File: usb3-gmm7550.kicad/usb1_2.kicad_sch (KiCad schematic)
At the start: 0 parts

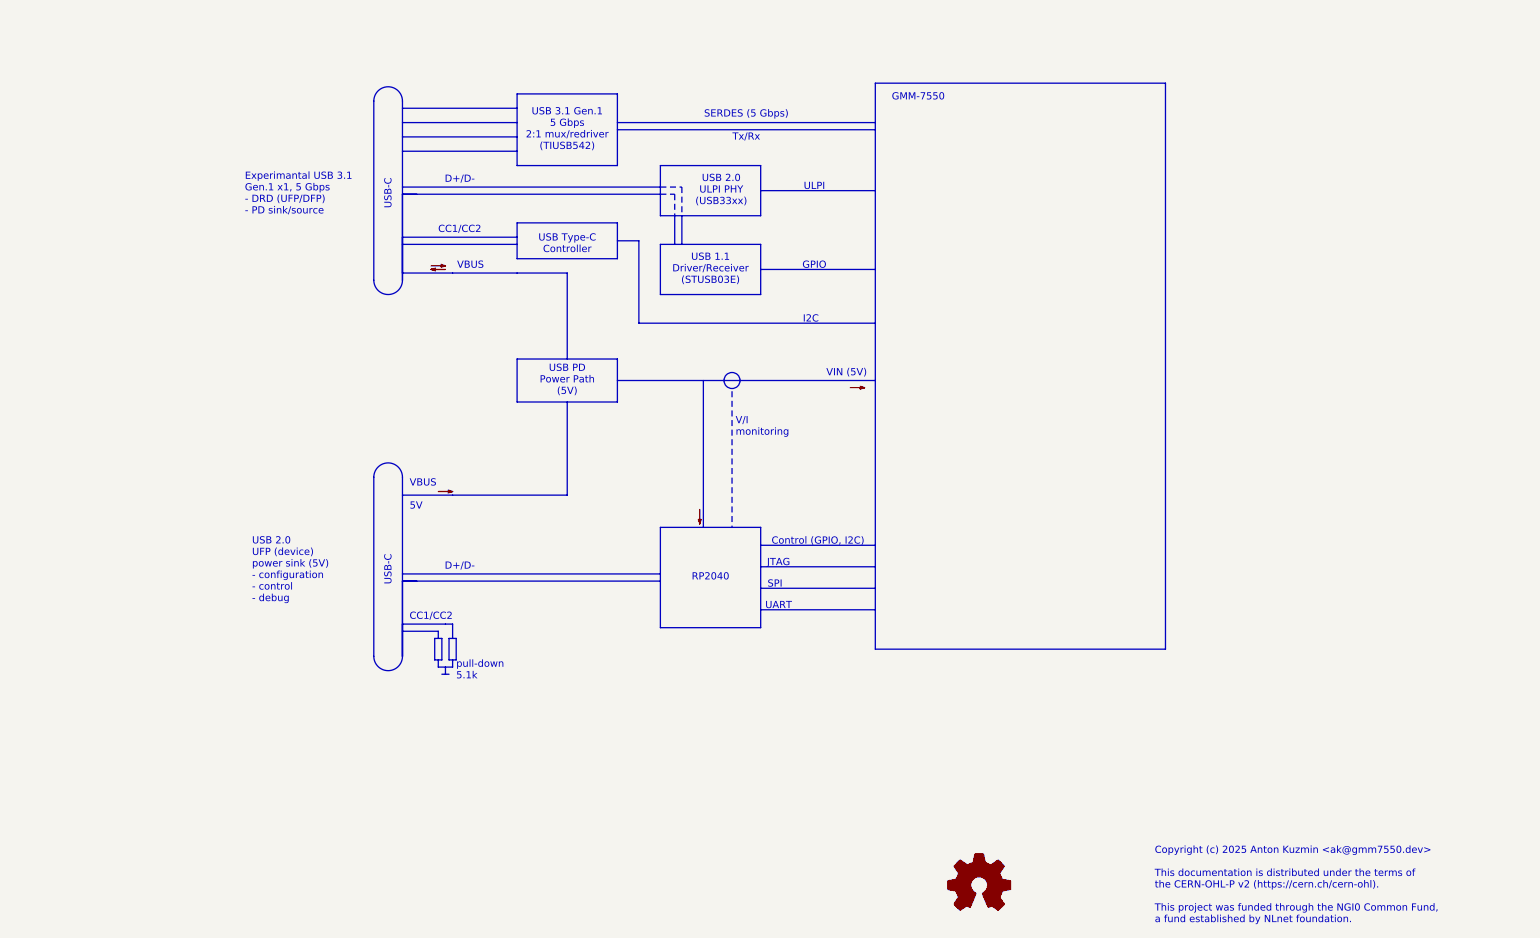
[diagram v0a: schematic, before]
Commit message: Add pages to the USB 3 Adapter schematic and new project symbols
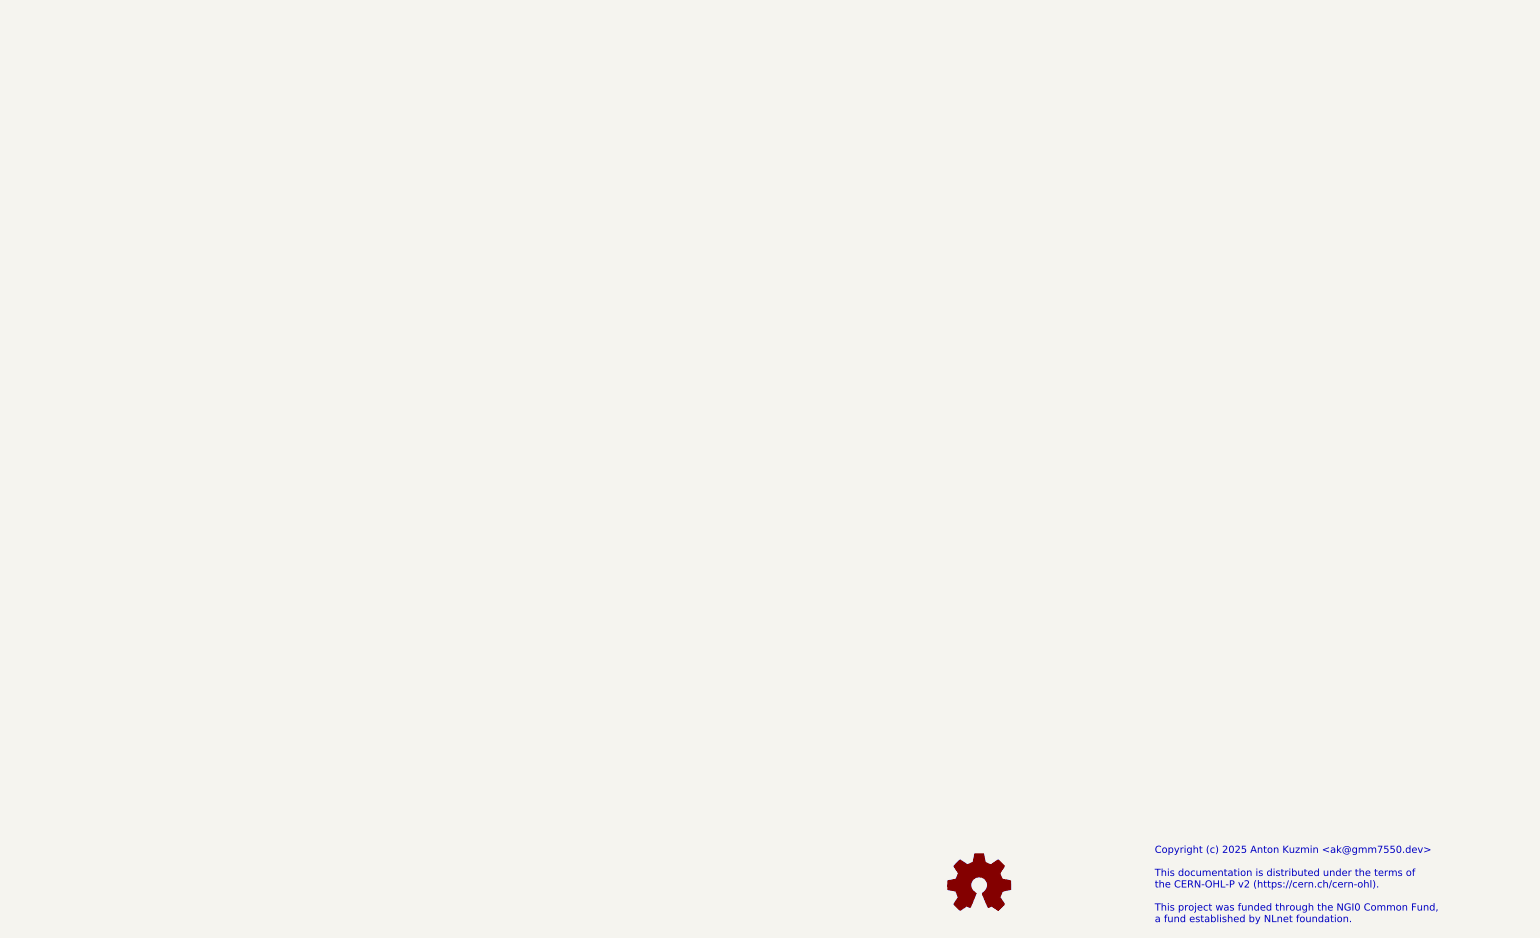
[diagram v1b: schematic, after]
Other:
- note removed: "CC1/CC2"
- note removed: "Control (GPIO, I2C)"
- note removed: "D+/D-"
- note removed: "Experimantal USB 3.1 Gen.1 x1, 5 Gbps - DRD (UFP/DFP) - PD sink/source"
- note removed: "GMM-7550"
- note removed: "GPIO"
- note removed: "I2C"
- note removed: "JTAG"
- note removed: "RP2040"
- note removed: "SERDES (5 Gbps) Tx/Rx"
- note removed: "SPI"
- note removed: "UART"
- note removed: "ULPI"
- note removed: "USB 1.1 Driver/Receiver (STUSB03E)"
- note removed: "USB 2.0 UFP (device) power sink (5V) - configuration - control - debug"
- note removed: "USB 2.0 ULPI PHY (USB33xx)"
- note removed: "USB 3.1 Gen.1 5 Gbps 2:1 mux/redriver (TIUSB542)"
- note removed: "USB PD Power Path (5V)"
- note removed: "USB Type-C Controller"
- note removed: "USB-C"
- note removed: "V/I monitoring"
- note removed: "VBUS"
- note removed: "VBUS 5V"
- note removed: "VIN (5V)"
- note removed: "pull-down 5.1k"

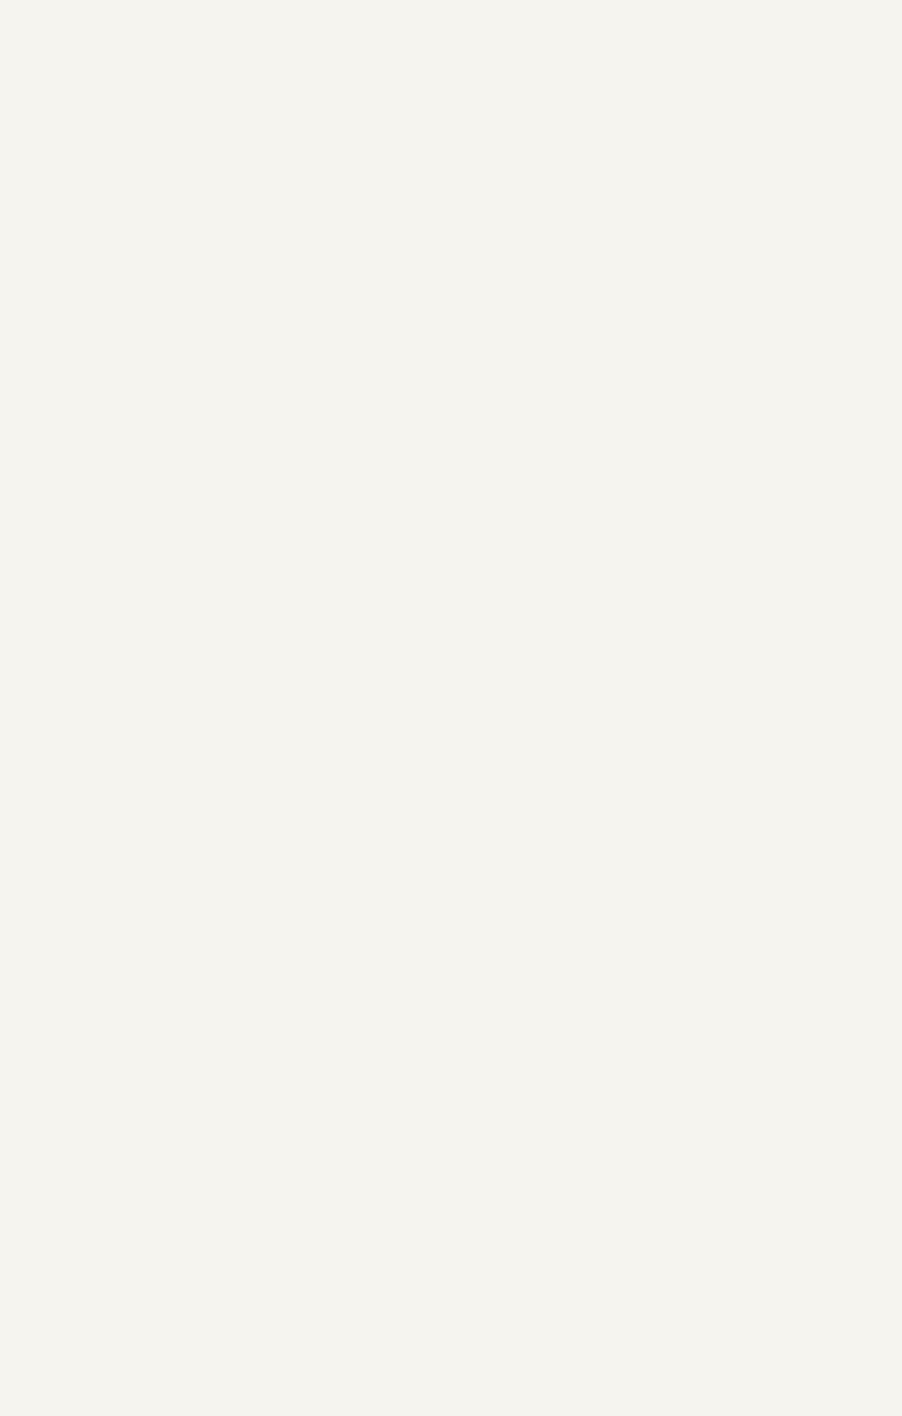
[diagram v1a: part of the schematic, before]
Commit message: USB 3 adapter schematic -- WIP
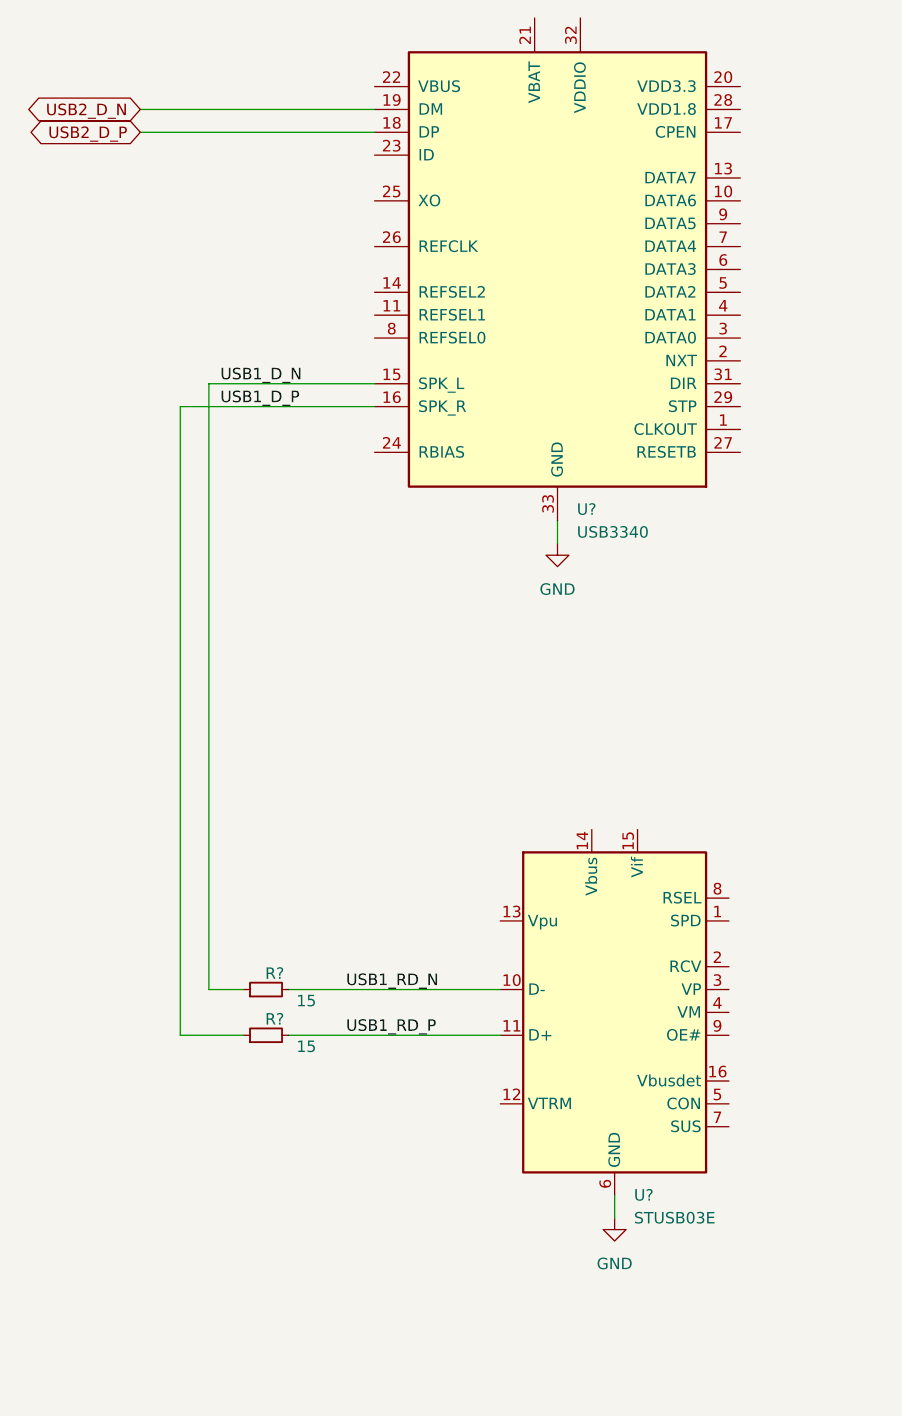
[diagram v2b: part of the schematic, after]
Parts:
- added R? (x2): 15, Resistor_SMD:R_0402_1005Metric, symbol Device:R_Small
- added U?: USB3340, Package_DFN_QFN:QFN-32-1EP_5x5mm_P0.5mm_EP3.3x3.3mm_ThermalVias, symbol usb3-gmm7550:USB3340
- added U?: STUSB03E, Package_DFN_QFN:QFN-16-1EP_3x3mm_P0.5mm_EP1.7x1.7mm, symbol Interface_USB:STUSB03E
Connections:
- new net GND: U?.33 (GND), U?.6 (GND)
- new net USB1_D_N: R?.1, U?.15 (SPK_L)
- new net USB1_D_P: R?.1, U?.16 (SPK_R)
- new net USB1_RD_N: R?.2, U?.10 (D-)
- new net USB1_RD_P: R?.2, U?.11 (D+)
- new net USB2_D_N: U?.19 (DM)
- new net USB2_D_P: U?.18 (DP)

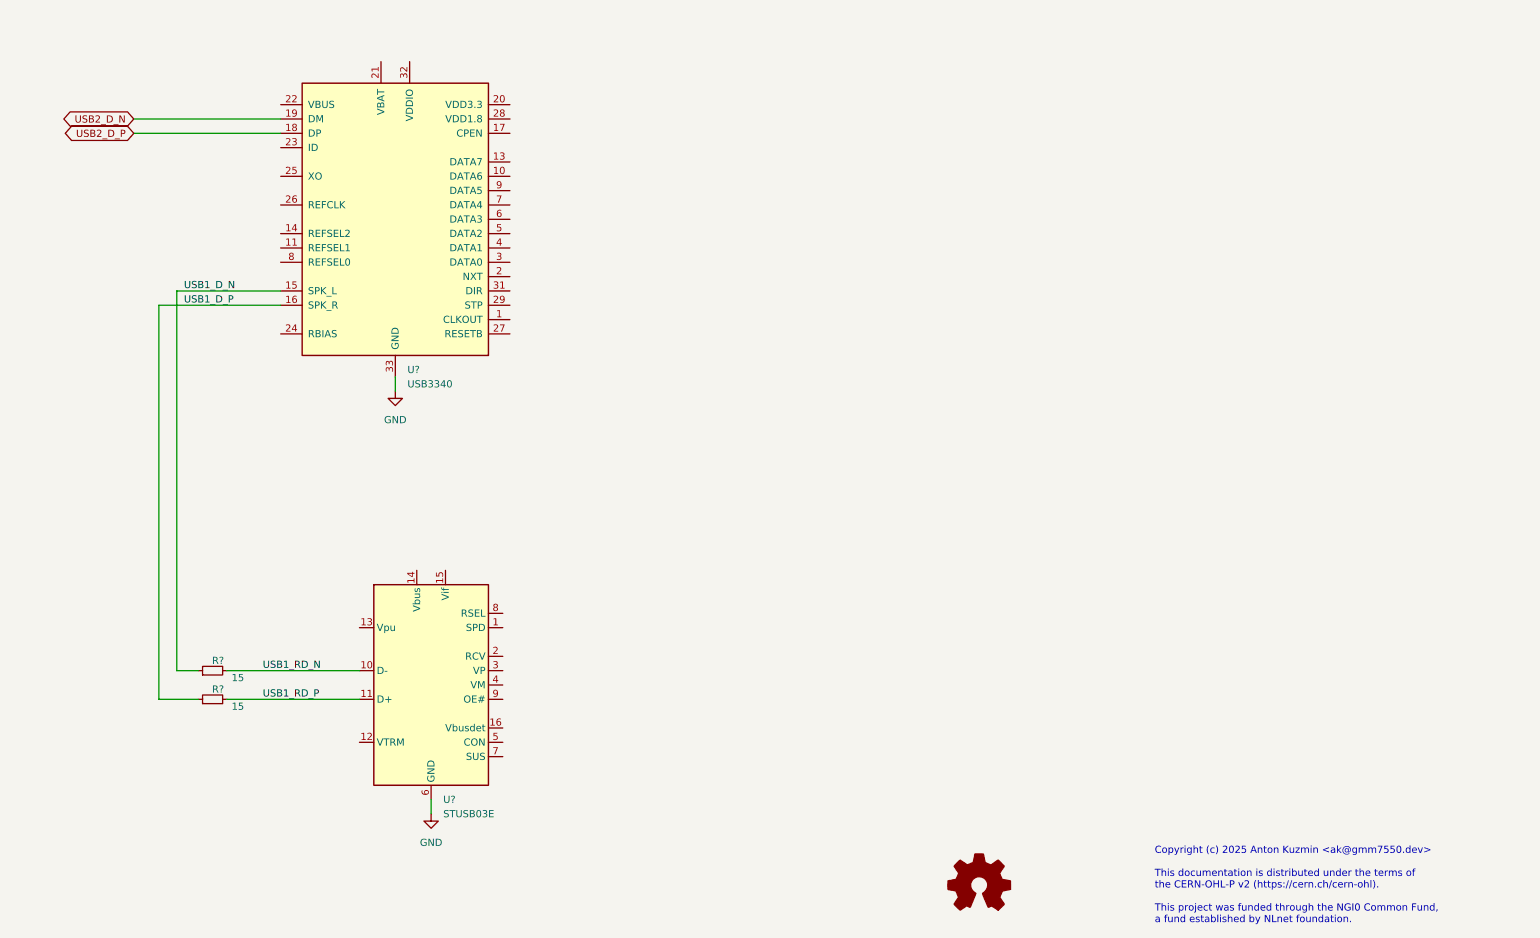
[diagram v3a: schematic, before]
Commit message: USB 3 adapter schematic -- WIP: USB 3 and Power Delivery pages
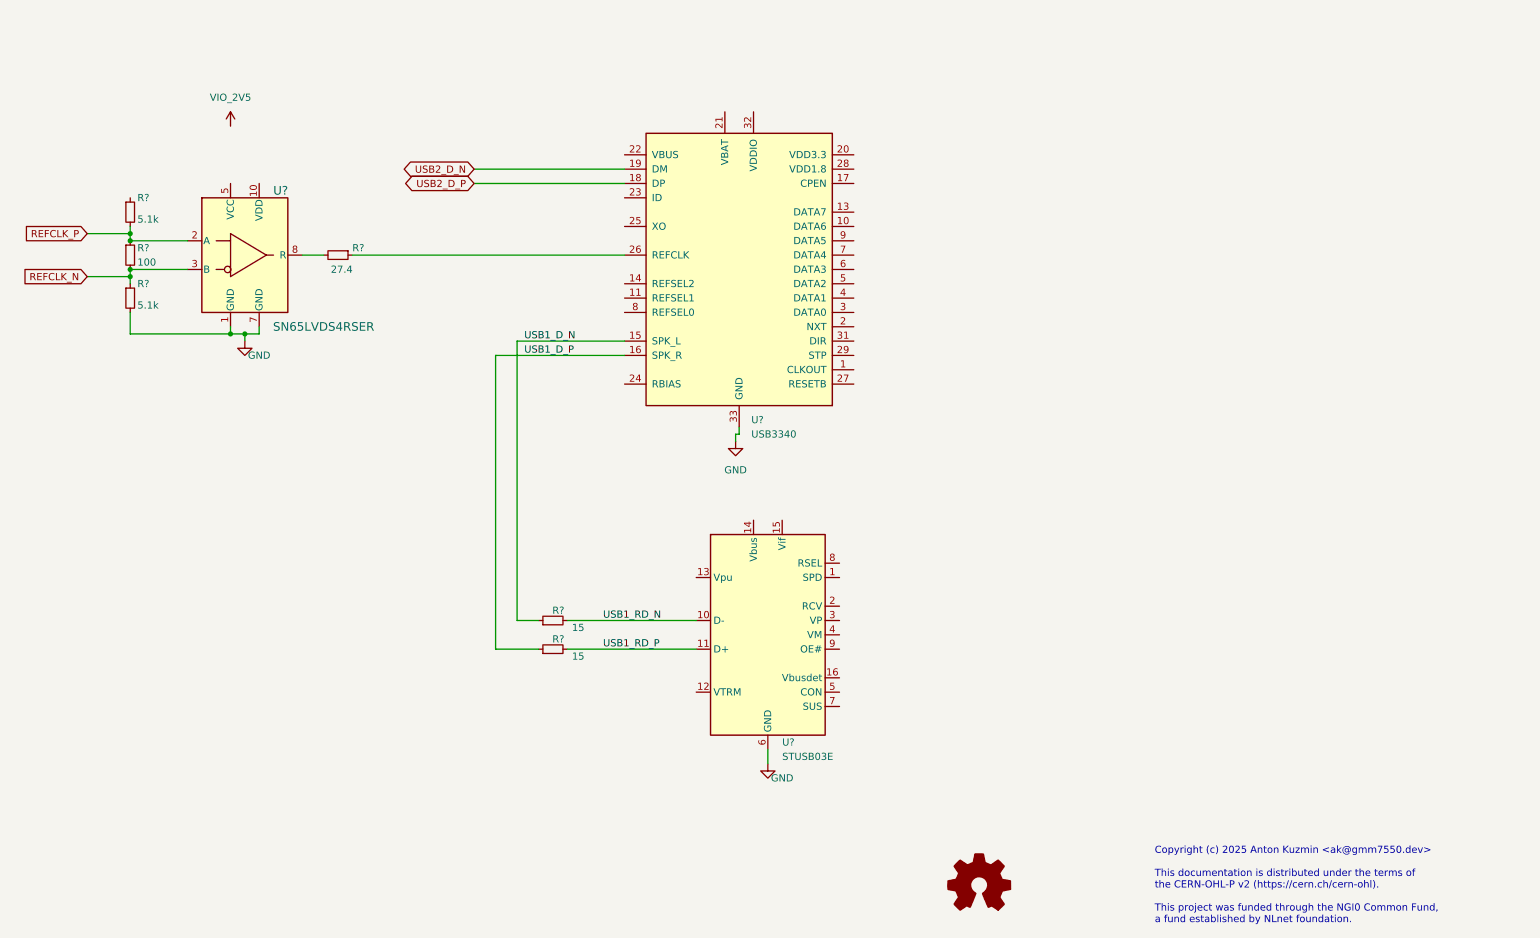
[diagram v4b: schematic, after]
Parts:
- added R?: 27.4, Resistor_SMD:R_0402_1005Metric, symbol Device:R_Small
- added R? (x2): 5.1k, Resistor_SMD:R_0402_1005Metric, symbol Device:R_Small
- added R?: 100, Resistor_SMD:R_0402_1005Metric, symbol Device:R_Small
- added U?: SN65LVDS4RSER, RSE10, symbol usb3-gmm7550:SN65LVDS4RSER
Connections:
- net GND: now also R?.2, U?.1 (GND), U?.7 (GND)
- net at U?.26 (REFCLK): now also R?.1
- new net: R?.2, U?.8 (R)
- new net REFCLK_N: R?.1, R?.2, U?.3 (B)
- new net REFCLK_P: R?.1, R?.2, U?.2 (A)
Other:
- moved on the sheet: R?, U?
